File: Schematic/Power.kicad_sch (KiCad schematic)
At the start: 37 parts, among them IC1 MP9943AGQ-Z, IC2 MP9943AGQ-Z, U2 ME6217C33M5G

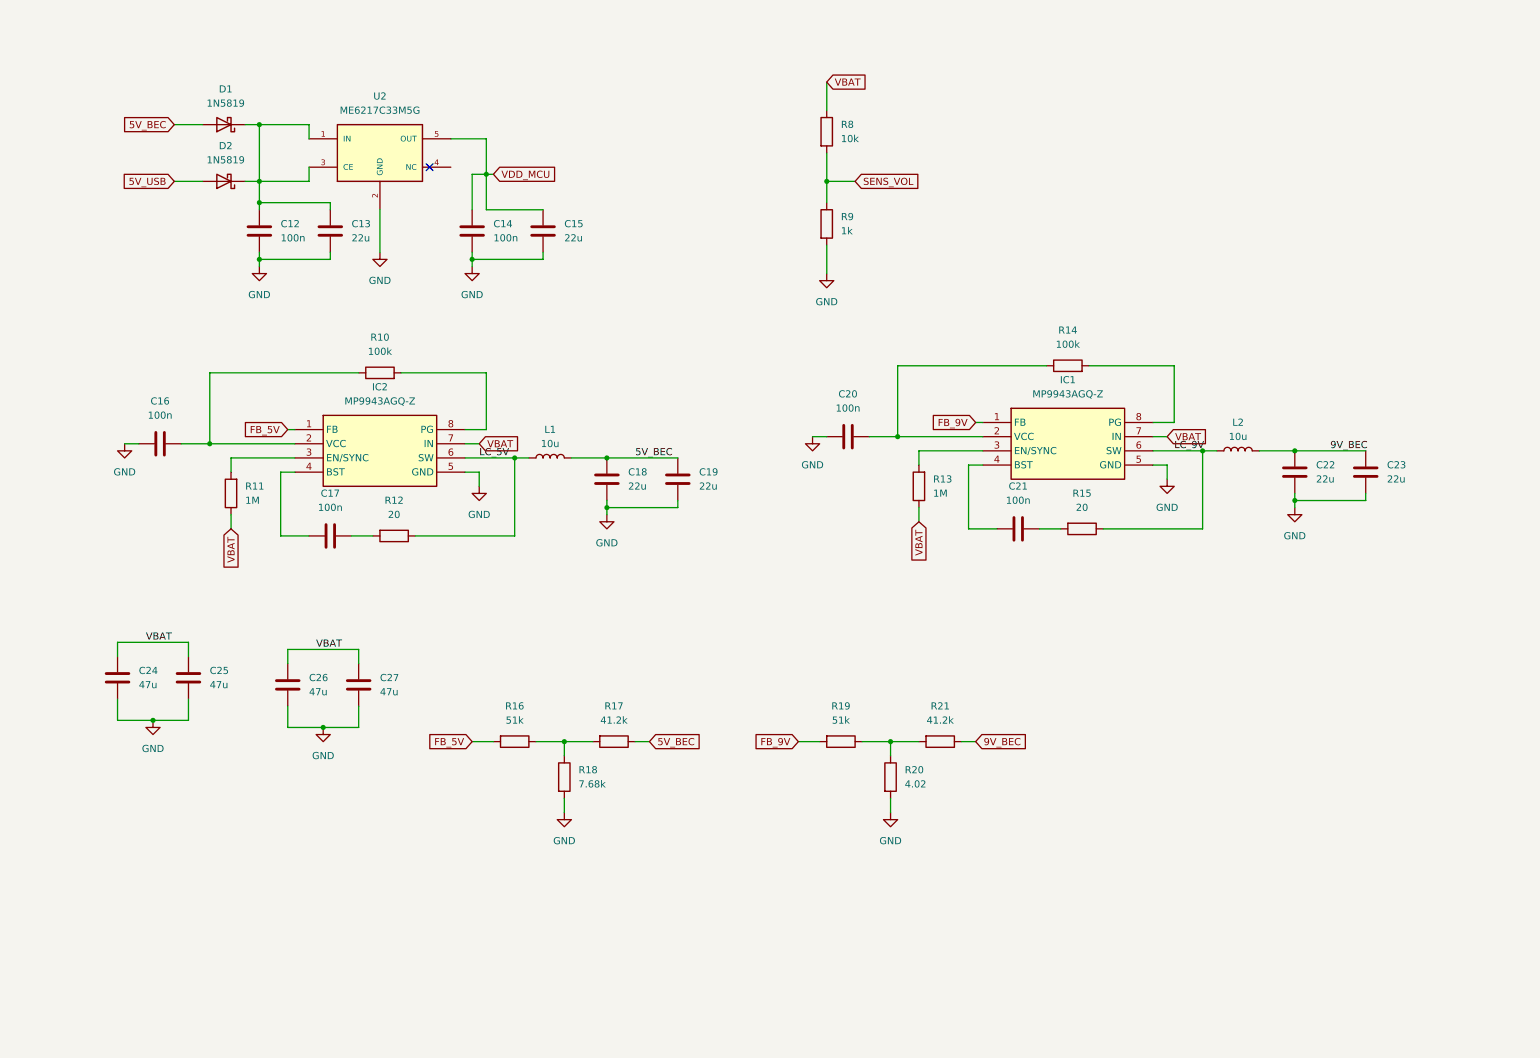
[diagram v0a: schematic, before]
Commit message: schematic fully finished, every footprint assigned, still electrical checking to do
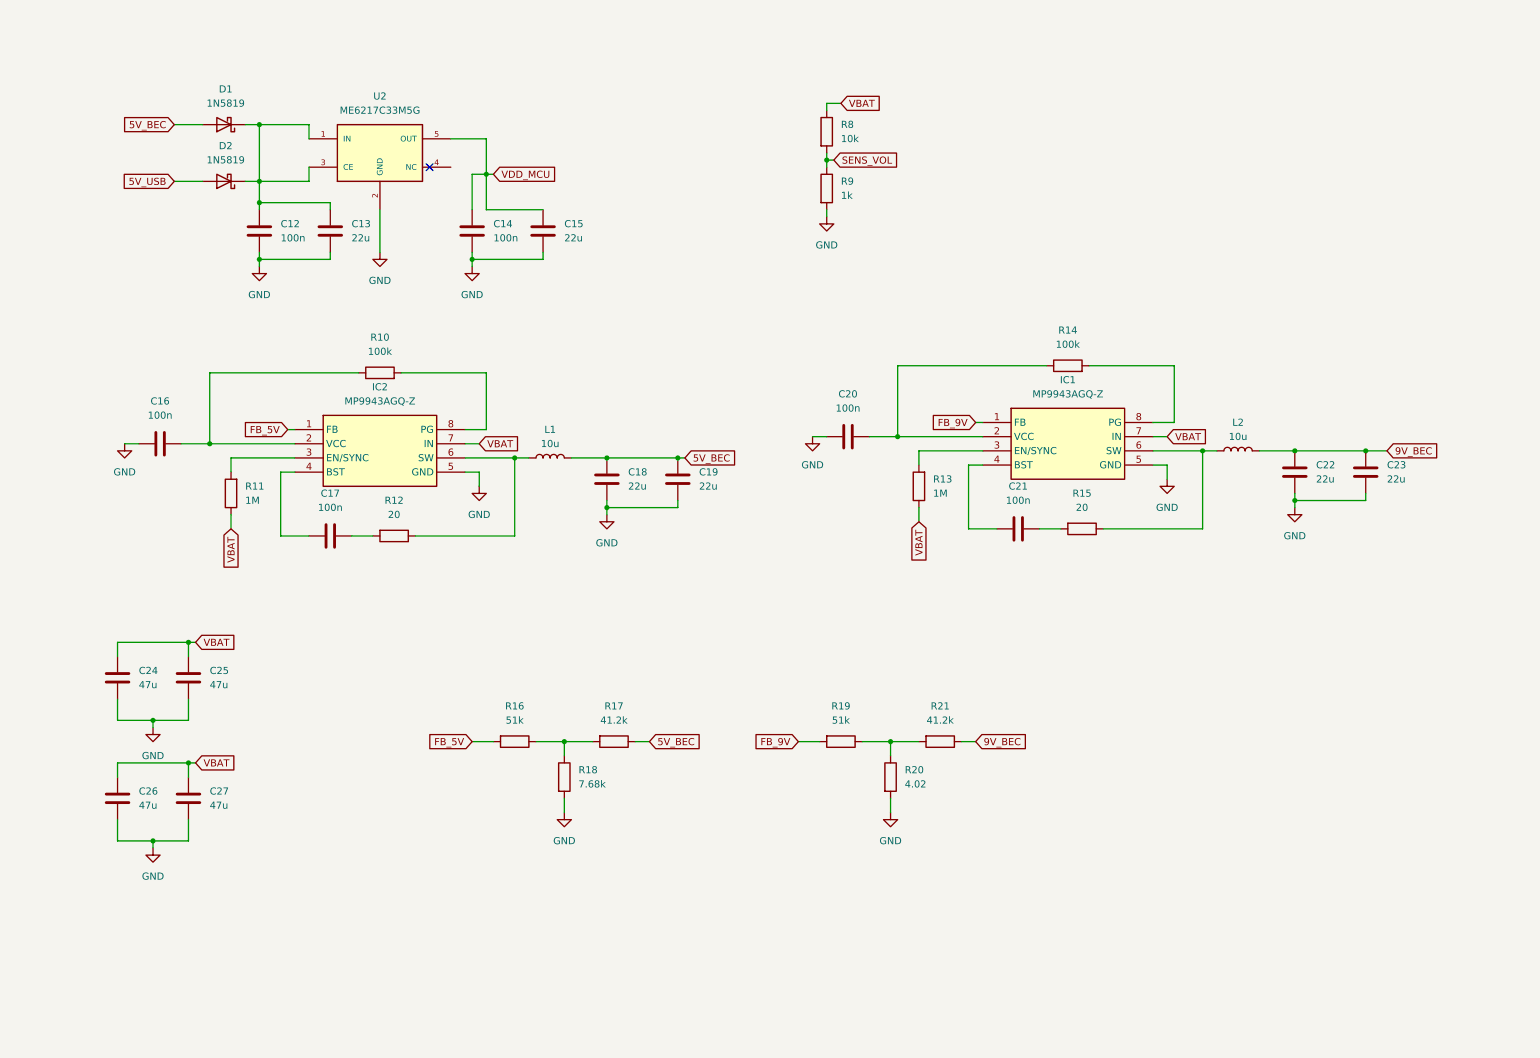
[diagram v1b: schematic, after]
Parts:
- IC1, IC2: footprint SON65P300X300X100-8N -> fch7_fp:SON65P300X300X100-8N
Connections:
- net LC_5V: no longer names the net of IC2.6 (SW), L1.1, R12.1
- net LC_9V: no longer names the net of IC1.6 (SW), L2.1, R15.1
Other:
- moved on the sheet: C26, C27, R9

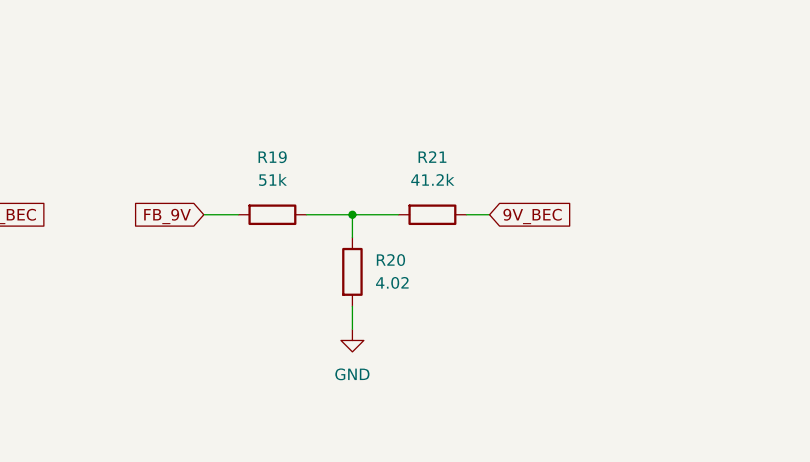
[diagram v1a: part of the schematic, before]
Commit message: reviewing and refactoring footprints and full schematic
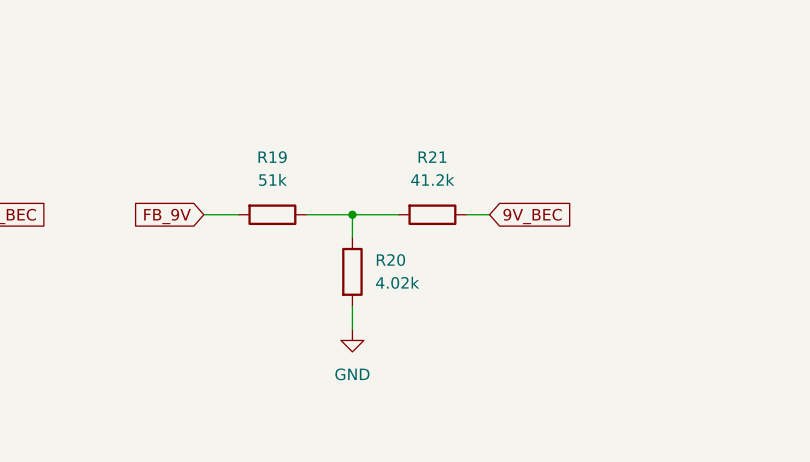
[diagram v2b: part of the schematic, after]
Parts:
- C12, C14, C16, C17, C20, C21: MPN (none) -> 0603B104K500NT; Manufacturer (none) -> FH
- C13, C15, C18, C19, C22, C23: footprint Capacitor_SMD:C_1210_3225Metric -> Capacitor_SMD:C_0805_2012Metric; MPN (none) -> CL21A226MAQNNNE; Manufacturer (none) -> SAMSUNG
- C24, C25, C26, C27: footprint Capacitor_SMD:C_1210_3225Metric -> Capacitor_SMD:C_1206_3216Metric; MPN (none) -> CL31A476MPHNNNE; Manufacturer (none) -> SAMSUNG
- D1, D2: MPN (none) -> 1N5819; Manufacturer (none) -> STM
- IC1, IC2: MPN (none) -> MP9943AGQ-Z; Manufacturer (none) -> MPS
- L1, L2: footprint Inductor_SMD:L_0805_2012Metric -> Inductor_SMD:L_Sunlord_MWSA0402S; MPN (none) -> FXL0420-100-M; Manufacturer (none) -> cjiang
- R10: MPN (none) -> RC0603FR-07100KL; Manufacturer (none) -> YAGEO
- R11, R13: MPN (none) -> 0603WAF1004T5E; Manufacturer (none) -> ROYALOHM
- R12, R15: MPN (none) -> 0603WAF200JT5E; Manufacturer (none) -> UNI-ROYAL
- R14: MPN (none) -> RC0603FR-07100KL; Manufacturer Yageo -> YAGEO
- R16, R19: MPN (none) -> 0603WAF5102T5E; Manufacturer (none) -> ROYALOHM
- R17, R21: MPN (none) -> 0603WAF4122T5E; Manufacturer (none) -> UNI-ROYAL
- R18: MPN (none) -> RS-03K7681FT; Manufacturer (none) -> FH
- R20: value 4.02 -> 4.02k; MPN (none) -> 0603WAF4021T5E; Manufacturer (none) -> UNI-ROYAL
- R8: MPN (none) -> 0603WAF1002T5E; Manufacturer (none) -> UNI-ROYAL
- R9: MPN (none) -> RC0603FR-071KL; Manufacturer (none) -> YAGEO
- U2: MPN (none) -> ME6217C33M5G; Manufacturer (none) -> MICRONE; Price None -> (none)

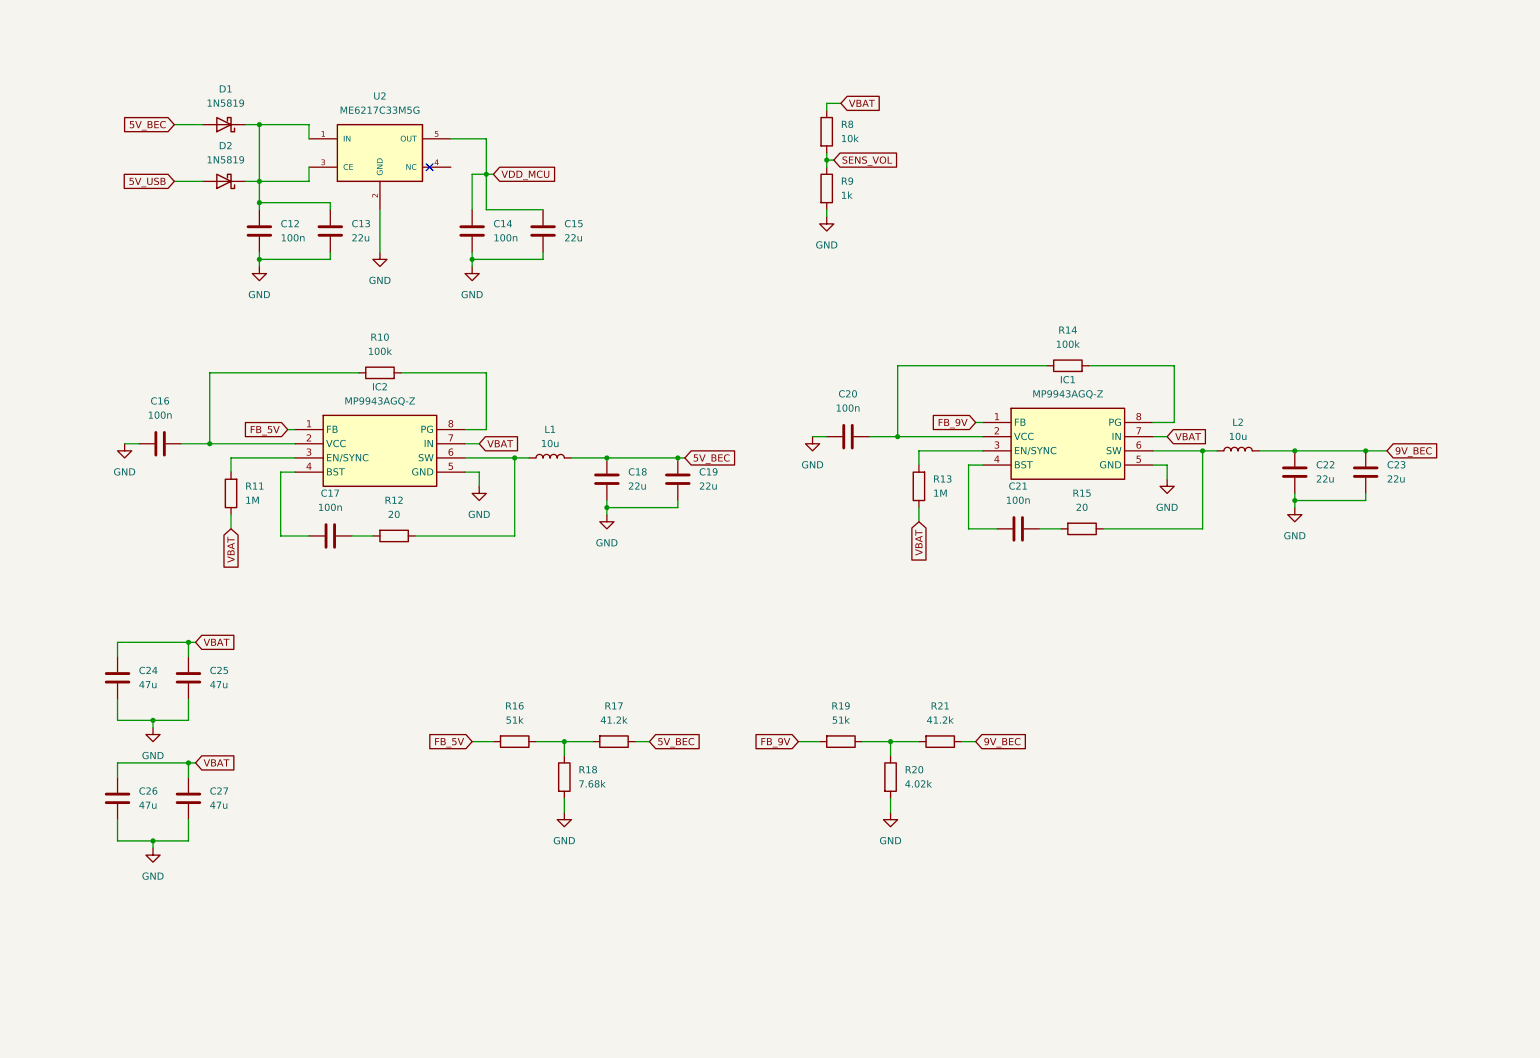
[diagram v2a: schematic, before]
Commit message: Update schematic and footprint libraries with various component modifications
- Updated fp-info-cache with new component details and footprint changes.
- Modified osd.kicad_sch to correct pin types and add no_connect entries.
- Adjusted rf_rx.kicad_sch to fix pin assignments and update component properties.
- Enhanced sensors.kicad_sch with new properties for QMC5883L and SPL06-001 sensors.
- Added new libraries to sym-lib-table and fp-lib-table for better organization and access to components.
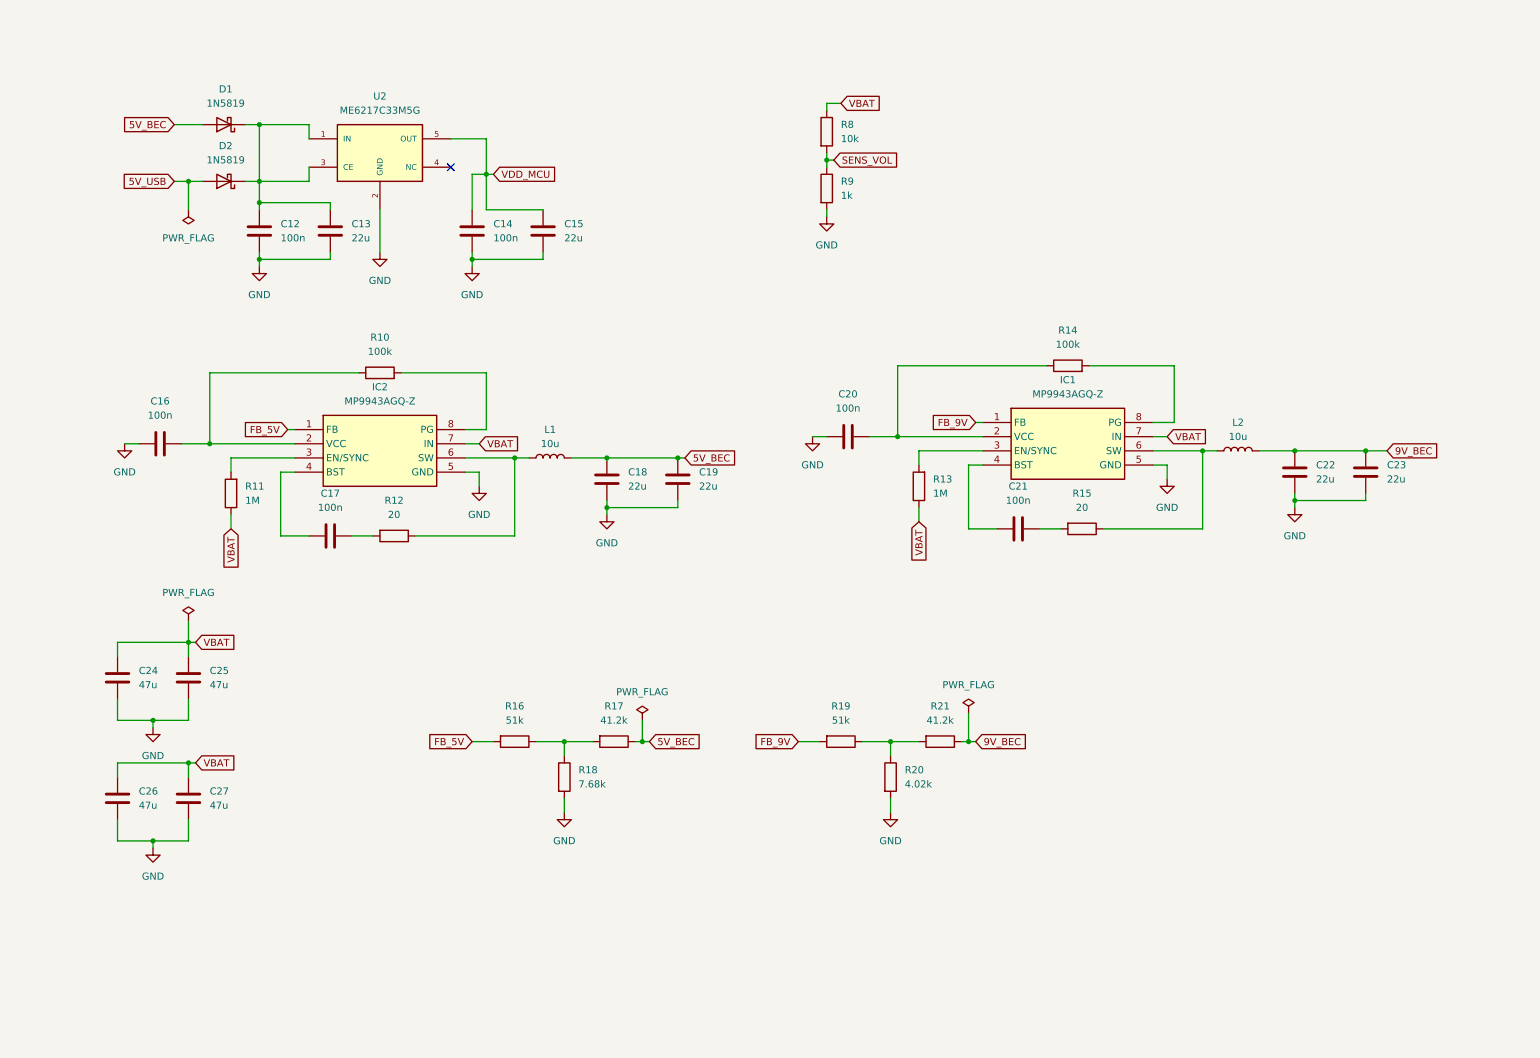
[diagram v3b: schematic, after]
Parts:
- U2: Price (none) -> None

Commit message: Refactor fp-lib-table: Remove unused libraries and update description for fch7_fp
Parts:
- U2: footprint ME6217C33M5G:SOT23-5 -> fch7_fp:SOT23-5
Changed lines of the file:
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@@
 			)
 		)
-		(property "Footprint" "ME6217C33M5G:SOT23-5"
+		(property "Footprint" "fch7_fp:SOT23-5"
 			(at 78.74 38.1 0)
 			(effects
